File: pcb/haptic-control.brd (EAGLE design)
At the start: 40 x 160 mm, 152 parts, among them M1 SPH0641LM4H-1, P1 2P-PAD_1X3.5, P2 2P-PAD_1X3.5, P3 2P-PAD_1X3.5, P4 2P-PAD_1X3.5, U1 MIC23159, U10 DRV2605L, U11 DRV2605L, U12 MTCH6301, U2 BQ51050B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

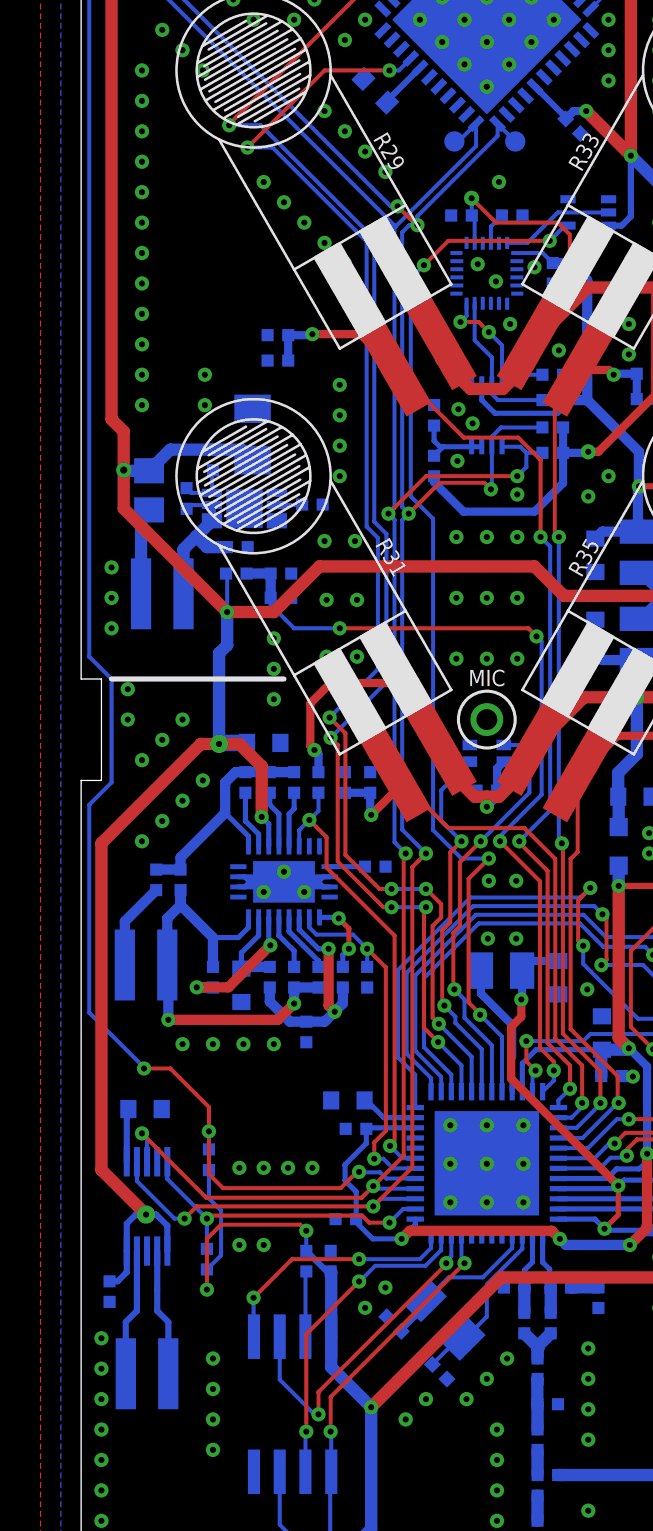
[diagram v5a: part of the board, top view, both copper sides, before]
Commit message: created a simplified bom for order
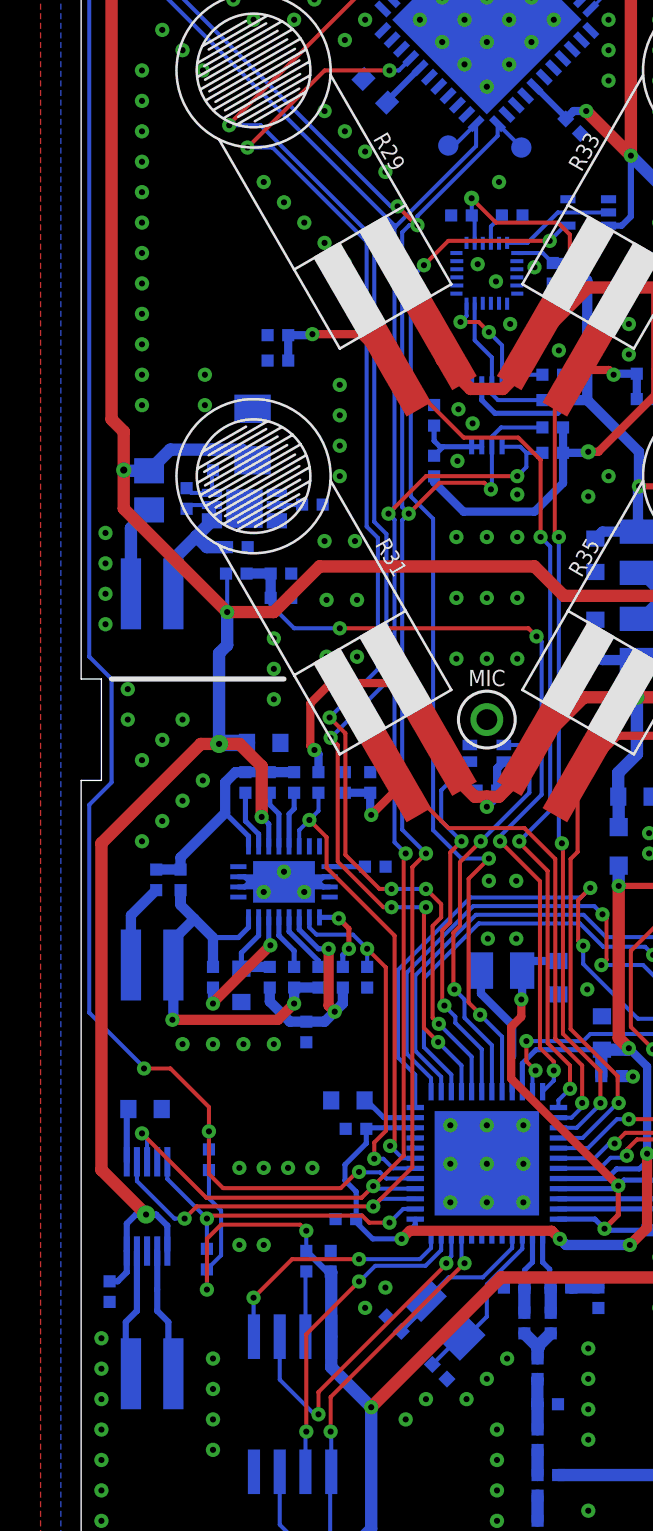
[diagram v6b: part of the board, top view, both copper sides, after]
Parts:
- moved LOGO1 0.72 mm to (28.9, 71.6)
- moved P2 0.50 mm to (3.50, 54.2)
- moved SCL 0.42 mm to (21.7, 76.2)
- moved SDA 0.36 mm to (18.1, 76.3)
- moved P1 0.30 mm to (3.50, 35.9)
- moved P3 0.25 mm to (3.50, 15.8)
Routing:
- net N$49: track 22.0 -> 21.3 mm
- net GND: vias 259 -> 260
